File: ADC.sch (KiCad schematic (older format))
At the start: 4 parts, among them J1 RCA, J2 RCA, P1 CONN_6, P2 CONN_6

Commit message: Completed component product code specification; started on footprints.
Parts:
- J1: DigiKey (none) -> CP-1414-ND
- J2: DigiKey (none) -> CP-1413-ND
- P1: DigiKey (none) -> SC1631-ND
- P2: DigiKey (none) -> SC1738-ND
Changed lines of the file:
@@
 LIBS:my-conn
 LIBS:ADC-cache
-EELAYER 27 0
+EELAYER 24 0
 EELAYER END
 $Descr A4 11693 8268
@@
 F 2 "" H 2500 4550 60  0000 C CNN
 F 3 "" H 2500 4550 60  0000 C CNN
+F 4 "SC1631-ND" V 2500 4550 60  0001 C CNN "DigiKey"
 	1    2500 4550
 	1    0    0    -1
@@
 F 2 "" H 2900 4550 60  0000 C CNN
 F 3 "" H 2900 4550 60  0000 C CNN
+F 4 "SC1738-ND" V 2900 4550 60  0001 C CNN "DigiKey"
 	1    2900 4550
 	-1   0    0    -1
@@
 F 2 "" H 5600 1900 60  0000 C CNN
 F 3 "" H 5600 1900 60  0000 C CNN
+F 4 "CP-1414-ND" H 5600 1900 60  0001 C CNN "DigiKey"
 	1    5600 1900
 	1    0    0    -1
@@
 F 2 "" H 5600 2750 60  0000 C CNN
 F 3 "" H 5600 2750 60  0000 C CNN
+F 4 "CP-1413-ND" H 5600 2750 60  0001 C CNN "DigiKey"
 	1    5600 2750
 	1    0    0    -1

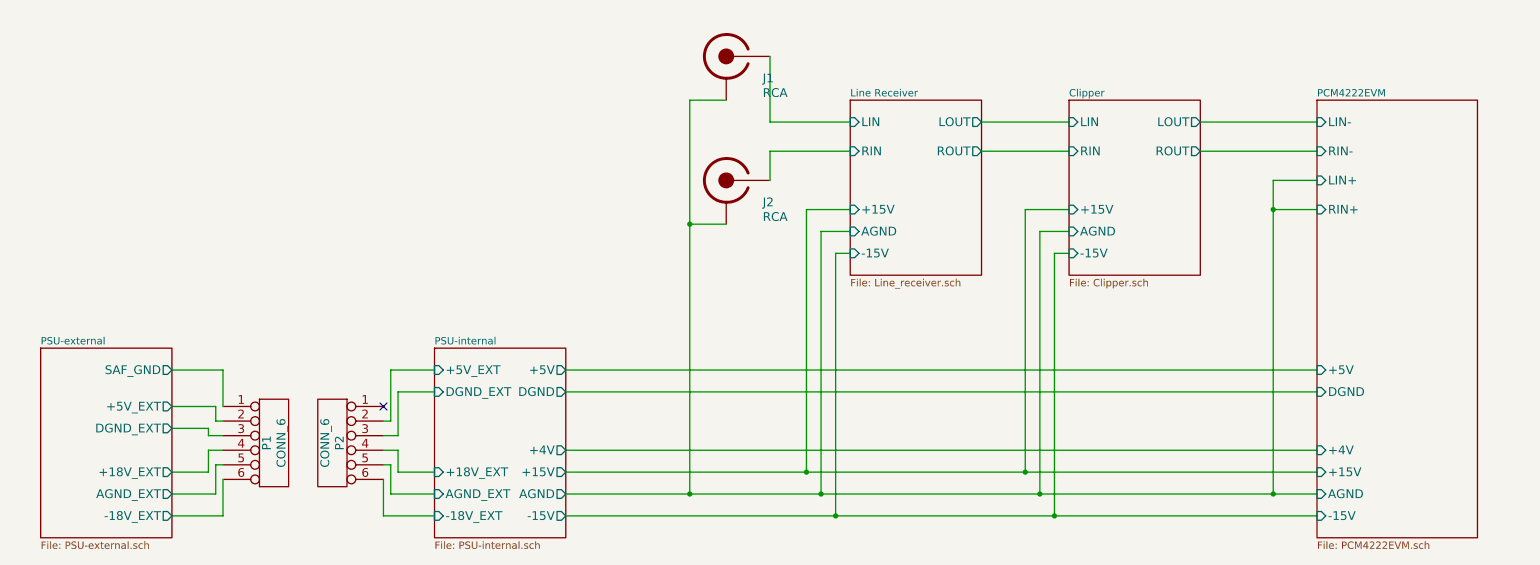
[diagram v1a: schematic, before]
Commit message: Added internal connectors; specified all footprints and part IDs except for the trafos.
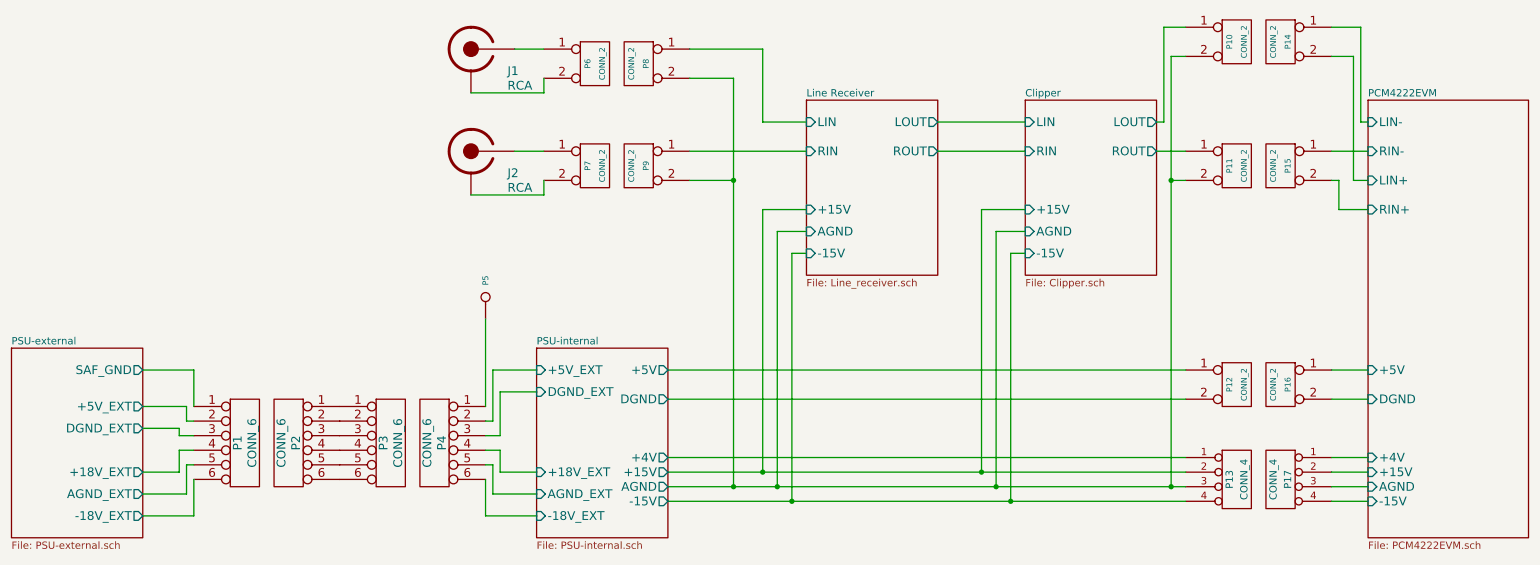
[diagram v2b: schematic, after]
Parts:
- added P10, P11, P12, P14, P15, P16, P6, P7, P8, P9: CONN_2, symbol CONN_2
- added P13, P17: CONN_4, symbol CONN_4
- added P3, P4: CONN_6, symbol CONN_6
- added P5: CONN_1, symbol CONN_1
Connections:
- net Clipper/+15V: now also P13.2 (P2)
- net Clipper/-15V: now also P13.4 (P4)
- net Clipper/AGND: now also P10.2 (PM), P11.2 (PM), P13.3 (P3), P8.2 (PM), P9.2 (PM); no longer J1.~, J2.~
- net Clipper/LOUT: now also P10.1 (P1)
- net Clipper/ROUT: now also P11.1 (P1)
- net Line Receiver/LIN: now also P8.1 (P1); no longer J1.~
- net Line Receiver/RIN: now also P9.1 (P1); no longer J2.~
- net PCM4222EVM/+4V: now also P17.1 (P1)
- net PCM4222EVM/+5V: now also P16.1 (P1)
- net PCM4222EVM/DGND: now also P16.2 (PM)
- net PSU-internal/+18V_EXT: now also P4.4; no longer P2.4
- net PSU-internal/+5V_EXT: now also P4.2; no longer P2.2
- net PSU-internal/-18V_EXT: now also P4.6; no longer P2.6
- net PSU-internal/AGND_EXT: now also P4.5; no longer P2.5
- net PSU-internal/DGND_EXT: now also P4.3; no longer P2.3
- net at P2.1: now also P3.1
- new net: P2.2, P3.2
- new net: P2.3, P3.3
- new net: P2.4, P3.4
- new net: P2.5, P3.5
- new net: P2.6, P3.6
- new net: J1.~, P6.1 (P1)
- new net: J1.~, P6.2 (PM)
- new net: J2.~, P7.1 (P1)
- new net: J2.~, P7.2 (PM)
- new net: P4.1, P5.1
- new net PCM4222EVM/+15V: P17.2 (P2)
- new net PCM4222EVM/-15V: P17.4 (P4)
- new net PCM4222EVM/AGND: P17.3 (P3)
- new net PCM4222EVM/LIN+: P14.2 (PM)
- new net PCM4222EVM/LIN-: P14.1 (P1)
- new net PCM4222EVM/RIN+: P15.2 (PM)
- new net PCM4222EVM/RIN-: P15.1 (P1)
- new net PSU-internal/+4V: P13.1 (P1)
- new net PSU-internal/+5V: P12.1 (P1)
- new net PSU-internal/DGND: P12.2 (PM)
- no-connect marks 1 -> 0
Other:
- moved on the sheet: J1, J2, P1, P2

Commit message: More footprint specification and connector additions; almost done.
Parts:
- P1, P2, P3, P4: footprint (none) -> Sockets_MOLEX_KK-System:Socket_MOLEX-KK-RM2-54mm_Lock_6pin_straight
- P10, P11, P12, P14, P15, P16, P6, P7, P8, P9: footprint (none) -> Sockets_MOLEX_KK-System:Socket_MOLEX-KK-RM2-54mm_Lock_2pin_straight
- P13, P17: footprint (none) -> Sockets_MOLEX_KK-System:Socket_MOLEX-KK-RM2-54mm_Lock_4pin_straight
- P5: footprint (none) -> Connect:1pin
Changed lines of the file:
@@
 F 0 "P1" V 2250 4550 60  0000 C CNN
 F 1 "CONN_6" V 2350 4550 60  0000 C CNN
-F 2 "" H 2300 4550 60  0000 C CNN
+F 2 "Sockets_MOLEX_KK-System:Socket_MOLEX-KK-RM2-54mm_Lock_6pin_straight" H 2300 4550 60  0001 C CNN
 F 3 "" H 2300 4550 60  0000 C CNN
 F 4 "SC1631-ND" V 2300 4550 60  0001 C CNN "DigiKey"
@@
 F 0 "P2" V 2550 4550 60  0000 C CNN
 F 1 "CONN_6" V 2650 4550 60  0000 C CNN
-F 2 "" H 2600 4550 60  0000 C CNN
+F 2 "Sockets_MOLEX_KK-System:Socket_MOLEX-KK-RM2-54mm_Lock_6pin_straight" H 2600 4550 60  0001 C CNN
 F 3 "" H 2600 4550 60  0000 C CNN
 F 4 "SC1738-ND" V 2600 4550 60  0001 C CNN "DigiKey"
@@
 F 0 "J1" H 4100 1700 60  0000 L CNN
 F 1 "RCA" H 4100 1600 60  0000 L CNN
-F 2 "" H 3850 1850 60  0000 C CNN
+F 2 "" H 3850 1850 60  0001 C CNN
 F 3 "" H 3850 1850 60  0000 C CNN
 F 4 "CP-1414-ND" H 3850 1850 60  0001 C CNN "DigiKey"
@@
 F 0 "J2" H 4100 2400 60  0000 L CNN
 F 1 "RCA" H 4100 2300 60  0000 L CNN
-F 2 "" H 3850 2550 60  0000 C CNN
+F 2 "" H 3850 2550 60  0001 C CNN
 F 3 "" H 3850 2550 60  0000 C CNN
 F 4 "CP-1413-ND" H 3850 2550 60  0001 C CNN "DigiKey"
@@
 F 0 "P6" V 4650 1950 40  0000 C CNN
 F 1 "CONN_2" V 4750 1950 40  0000 C CNN
-F 2 "" H 4700 1950 60  0000 C CNN
+F 2 "Sockets_MOLEX_KK-System:Socket_MOLEX-KK-RM2-54mm_Lock_2pin_straight" H 4700 1950 60  0001 C CNN
 F 3 "" H 4700 1950 60  0000 C CNN
 F 4 "WM2011-ND" V 4700 1950 60  0001 C CNN "DigiKey"
@@
 F 0 "P7" V 4650 2650 40  0000 C CNN
 F 1 "CONN_2" V 4750 2650 40  0000 C CNN
-F 2 "" H 4700 2650 60  0000 C CNN
+F 2 "Sockets_MOLEX_KK-System:Socket_MOLEX-KK-RM2-54mm_Lock_2pin_straight" H 4700 2650 60  0001 C CNN
 F 3 "" H 4700 2650 60  0000 C CNN
 F 4 "WM2011-ND" V 4700 2650 60  0001 C CNN "DigiKey"
@@
 F 0 "P9" V 4950 2650 40  0000 C CNN
 F 1 "CONN_2" V 5050 2650 40  0000 C CNN
-F 2 "" H 5000 2650 60  0000 C CNN
+F 2 "Sockets_MOLEX_KK-System:Socket_MOLEX-KK-RM2-54mm_Lock_2pin_straight" H 5000 2650 60  0001 C CNN
 F 3 "" H 5000 2650 60  0000 C CNN
 F 4 "WM4200-ND" V 5000 2650 60  0001 C CNN "DigiKey"
@@
 F 0 "P8" V 4950 1950 40  0000 C CNN
 F 1 "CONN_2" V 5050 1950 40  0000 C CNN
-F 2 "" H 5000 1950 60  0000 C CNN
+F 2 "Sockets_MOLEX_KK-System:Socket_MOLEX-KK-RM2-54mm_Lock_2pin_straight" H 5000 1950 60  0001 C CNN
 F 3 "" H 5000 1950 60  0000 C CNN
 F 4 "WM4200-ND" V 5000 1950 60  0001 C CNN "DigiKey"
@@
 F 0 "P5" H 4030 3550 40  0000 L CNN
 F 1 "CONN_1" H 3950 3605 30  0001 C CNN
-F 2 "" H 3950 3550 60  0000 C CNN
+F 2 "Connect:1pin" H 3950 3550 60  0001 C CNN
 F 3 "" H 3950 3550 60  0000 C CNN
 	1    3950 3550
@@
 F 0 "P10" V 9050 1800 40  0000 C CNN
 F 1 "CONN_2" V 9150 1800 40  0000 C CNN
-F 2 "" H 9100 1800 60  0000 C CNN
+F 2 "Sockets_MOLEX_KK-System:Socket_MOLEX-KK-RM2-54mm_Lock_2pin_straight" H 9100 1800 60  0001 C CNN
 F 3 "" H 9100 1800 60  0000 C CNN
 F 4 "WM4200-ND" V 9100 1800 60  0001 C CNN "DigiKey"
@@
 F 0 "P14" V 9350 1800 40  0000 C CNN
 F 1 "CONN_2" V 9450 1800 40  0000 C CNN
-F 2 "" H 9400 1800 60  0000 C CNN
+F 2 "Sockets_MOLEX_KK-System:Socket_MOLEX-KK-RM2-54mm_Lock_2pin_straight" H 9400 1800 60  0001 C CNN
 F 3 "" H 9400 1800 60  0000 C CNN
 F 4 "WM2011-ND" V 9400 1800 60  0001 C CNN "DigiKey"
@@
 F 0 "P12" V 9050 4150 40  0000 C CNN
 F 1 "CONN_2" V 9150 4150 40  0000 C CNN
-F 2 "" H 9100 4150 60  0000 C CNN
+F 2 "Sockets_MOLEX_KK-System:Socket_MOLEX-KK-RM2-54mm_Lock_2pin_straight" H 9100 4150 60  0001 C CNN
 F 3 "" H 9100 4150 60  0000 C CNN
 F 4 "WM4200-ND" V 9100 4150 60  0001 C CNN "DigiKey"
@@
 F 0 "P15" V 9350 2650 40  0000 C CNN
 F 1 "CONN_2" V 9450 2650 40  0000 C CNN
-F 2 "" H 9400 2650 60  0000 C CNN
+F 2 "Sockets_MOLEX_KK-System:Socket_MOLEX-KK-RM2-54mm_Lock_2pin_straight" H 9400 2650 60  0001 C CNN
 F 3 "" H 9400 2650 60  0000 C CNN
 F 4 "WM2011-ND" V 9400 2650 60  0001 C CNN "DigiKey"
@@
 F 0 "P16" V 9350 4150 40  0000 C CNN
 F 1 "CONN_2" V 9450 4150 40  0000 C CNN
-F 2 "" H 9400 4150 60  0000 C CNN
+F 2 "Sockets_MOLEX_KK-System:Socket_MOLEX-KK-RM2-54mm_Lock_2pin_straight" H 9400 4150 60  0001 C CNN
 F 3 "" H 9400 4150 60  0000 C CNN
 F 4 "WM2011-ND" V 9400 4150 60  0001 C CNN "DigiKey"
@@
 F 0 "P11" V 9050 2650 40  0000 C CNN
 F 1 "CONN_2" V 9150 2650 40  0000 C CNN
-F 2 "" H 9100 2650 60  0000 C CNN
+F 2 "Sockets_MOLEX_KK-System:Socket_MOLEX-KK-RM2-54mm_Lock_2pin_straight" H 9100 2650 60  0001 C CNN
 F 3 "" H 9100 2650 60  0000 C CNN
 F 4 "WM4200-ND" V 9100 2650 60  0001 C CNN "DigiKey"
@@
 F 0 "P13" V 9050 4800 50  0000 C CNN
 F 1 "CONN_4" V 9150 4800 50  0000 C CNN
-F 2 "" H 9100 4800 60  0000 C CNN
+F 2 "Sockets_MOLEX_KK-System:Socket_MOLEX-KK-RM2-54mm_Lock_4pin_straight" H 9100 4800 60  0001 C CNN
 F 3 "" H 9100 4800 60  0000 C CNN
 F 4 "WM4202-ND" V 9100 4800 60  0001 C CNN "DigiKey"
@@
 F 0 "P17" V 9350 4800 50  0000 C CNN
 F 1 "CONN_4" V 9450 4800 50  0000 C CNN
-F 2 "" H 9400 4800 60  0000 C CNN
+F 2 "Sockets_MOLEX_KK-System:Socket_MOLEX-KK-RM2-54mm_Lock_4pin_straight" H 9400 4800 60  0001 C CNN
 F 3 "" H 9400 4800 60  0000 C CNN
 F 4 "WM2603-ND" V 9400 4800 60  0001 C CNN "DigiKey"
@@
 F 0 "P4" V 3550 4550 60  0000 C CNN
 F 1 "CONN_6" V 3650 4550 60  0000 C CNN
-F 2 "" H 3600 4550 60  0000 C CNN
+F 2 "Sockets_MOLEX_KK-System:Socket_MOLEX-KK-RM2-54mm_Lock_6pin_straight" H 3600 4550 60  0001 C CNN
 F 3 "" H 3600 4550 60  0000 C CNN
 F 4 "WM4204-ND" V 3600 4550 60  0001 C CNN "DigiKey"
@@
 F 0 "P3" V 3250 4550 60  0000 C CNN
 F 1 "CONN_6" V 3350 4550 60  0000 C CNN
-F 2 "" H 3300 4550 60  0000 C CNN
+F 2 "Sockets_MOLEX_KK-System:Socket_MOLEX-KK-RM2-54mm_Lock_6pin_straight" H 3300 4550 60  0001 C CNN
 F 3 "" H 3300 4550 60  0000 C CNN
 F 4 "WM2015-ND" V 3300 4550 60  0001 C CNN "DigiKey"

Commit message: Changed to use the fixed IEC socket device; the PSU netlist should now be (more) correct.
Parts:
- J1, J2: footprint (none) -> Oddities:Dummy_Empty
- P14, P15, P16, P6, P7: footprint Sockets_MOLEX_KK-System:Socket_MOLEX-KK-RM2-54mm_Lock_2pin_straight -> Oddities:Dummy_Empty
- P17: footprint Sockets_MOLEX_KK-System:Socket_MOLEX-KK-RM2-54mm_Lock_4pin_straight -> Oddities:Dummy_Empty
- P2, P3: footprint Sockets_MOLEX_KK-System:Socket_MOLEX-KK-RM2-54mm_Lock_6pin_straight -> Oddities:Dummy_Empty
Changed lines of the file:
@@
 F 0 "P2" V 2550 4550 60  0000 C CNN
 F 1 "CONN_6" V 2650 4550 60  0000 C CNN
-F 2 "Sockets_MOLEX_KK-System:Socket_MOLEX-KK-RM2-54mm_Lock_6pin_straight" H 2600 4550 60  0001 C CNN
+F 2 "Oddities:Dummy_Empty" H 2600 4550 60  0001 C CNN
 F 3 "" H 2600 4550 60  0000 C CNN
 F 4 "SC1738-ND" V 2600 4550 60  0001 C CNN "DigiKey"
@@
 F 0 "J1" H 4100 1700 60  0000 L CNN
 F 1 "RCA" H 4100 1600 60  0000 L CNN
-F 2 "" H 3850 1850 60  0001 C CNN
+F 2 "Oddities:Dummy_Empty" H 3850 1850 60  0001 C CNN
 F 3 "" H 3850 1850 60  0000 C CNN
 F 4 "CP-1414-ND" H 3850 1850 60  0001 C CNN "DigiKey"
@@
 F 0 "J2" H 4100 2400 60  0000 L CNN
 F 1 "RCA" H 4100 2300 60  0000 L CNN
-F 2 "" H 3850 2550 60  0001 C CNN
+F 2 "Oddities:Dummy_Empty" H 3850 2550 60  0001 C CNN
 F 3 "" H 3850 2550 60  0000 C CNN
 F 4 "CP-1413-ND" H 3850 2550 60  0001 C CNN "DigiKey"
@@
 F 0 "P6" V 4650 1950 40  0000 C CNN
 F 1 "CONN_2" V 4750 1950 40  0000 C CNN
-F 2 "Sockets_MOLEX_KK-System:Socket_MOLEX-KK-RM2-54mm_Lock_2pin_straight" H 4700 1950 60  0001 C CNN
+F 2 "Oddities:Dummy_Empty" H 4700 1950 60  0001 C CNN
 F 3 "" H 4700 1950 60  0000 C CNN
 F 4 "WM2011-ND" V 4700 1950 60  0001 C CNN "DigiKey"
@@
 F 0 "P7" V 4650 2650 40  0000 C CNN
 F 1 "CONN_2" V 4750 2650 40  0000 C CNN
-F 2 "Sockets_MOLEX_KK-System:Socket_MOLEX-KK-RM2-54mm_Lock_2pin_straight" H 4700 2650 60  0001 C CNN
+F 2 "Oddities:Dummy_Empty" H 4700 2650 60  0001 C CNN
 F 3 "" H 4700 2650 60  0000 C CNN
 F 4 "WM2011-ND" V 4700 2650 60  0001 C CNN "DigiKey"
@@
 F 0 "P14" V 9350 1800 40  0000 C CNN
 F 1 "CONN_2" V 9450 1800 40  0000 C CNN
-F 2 "Sockets_MOLEX_KK-System:Socket_MOLEX-KK-RM2-54mm_Lock_2pin_straight" H 9400 1800 60  0001 C CNN
+F 2 "Oddities:Dummy_Empty" H 9400 1800 60  0001 C CNN
 F 3 "" H 9400 1800 60  0000 C CNN
 F 4 "WM2011-ND" V 9400 1800 60  0001 C CNN "DigiKey"
@@
 F 0 "P15" V 9350 2650 40  0000 C CNN
 F 1 "CONN_2" V 9450 2650 40  0000 C CNN
-F 2 "Sockets_MOLEX_KK-System:Socket_MOLEX-KK-RM2-54mm_Lock_2pin_straight" H 9400 2650 60  0001 C CNN
+F 2 "Oddities:Dummy_Empty" H 9400 2650 60  0001 C CNN
 F 3 "" H 9400 2650 60  0000 C CNN
 F 4 "WM2011-ND" V 9400 2650 60  0001 C CNN "DigiKey"
@@
 F 0 "P16" V 9350 4150 40  0000 C CNN
 F 1 "CONN_2" V 9450 4150 40  0000 C CNN
-F 2 "Sockets_MOLEX_KK-System:Socket_MOLEX-KK-RM2-54mm_Lock_2pin_straight" H 9400 4150 60  0001 C CNN
+F 2 "Oddities:Dummy_Empty" H 9400 4150 60  0001 C CNN
 F 3 "" H 9400 4150 60  0000 C CNN
 F 4 "WM2011-ND" V 9400 4150 60  0001 C CNN "DigiKey"
@@
 F 0 "P17" V 9350 4800 50  0000 C CNN
 F 1 "CONN_4" V 9450 4800 50  0000 C CNN
-F 2 "Sockets_MOLEX_KK-System:Socket_MOLEX-KK-RM2-54mm_Lock_4pin_straight" H 9400 4800 60  0001 C CNN
+F 2 "Oddities:Dummy_Empty" H 9400 4800 60  0001 C CNN
 F 3 "" H 9400 4800 60  0000 C CNN
 F 4 "WM2603-ND" V 9400 4800 60  0001 C CNN "DigiKey"
@@
 F 0 "P3" V 3250 4550 60  0000 C CNN
 F 1 "CONN_6" V 3350 4550 60  0000 C CNN
-F 2 "Sockets_MOLEX_KK-System:Socket_MOLEX-KK-RM2-54mm_Lock_6pin_straight" H 3300 4550 60  0001 C CNN
+F 2 "Oddities:Dummy_Empty" H 3300 4550 60  0001 C CNN
 F 3 "" H 3300 4550 60  0000 C CNN
 F 4 "WM2015-ND" V 3300 4550 60  0001 C CNN "DigiKey"

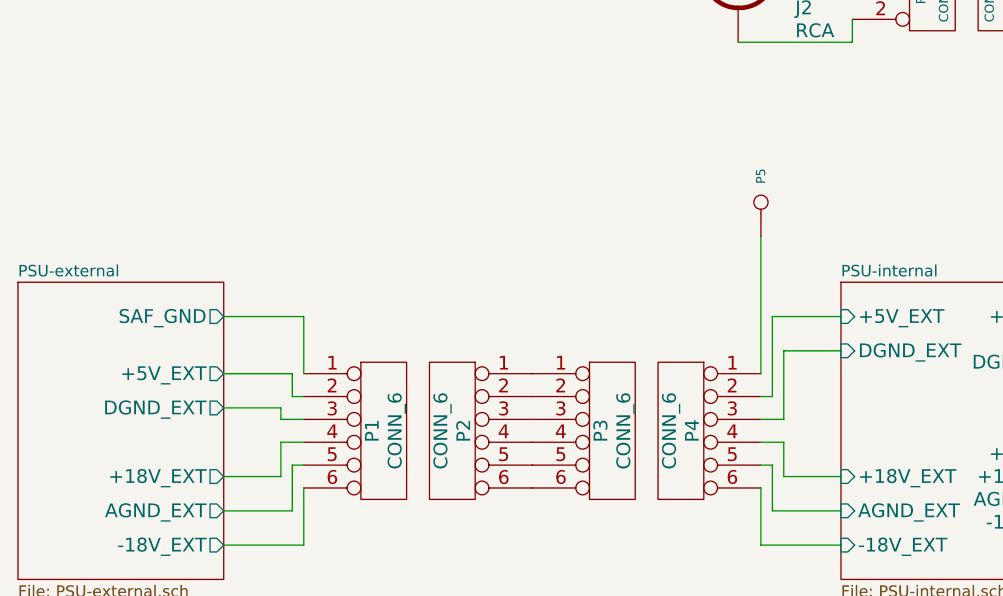
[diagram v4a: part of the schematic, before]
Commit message: A lot of routing, some parts changes:   * Added snubber C/RC snubbers to transformer secondaries.   * Changed PSU OA from OPA209 to OPA27.   * Routed external PSU.   * Mostly done routing internal circuits.  Just need to get everything together.   * Changed digital transformer to a more appropriately-specced one.
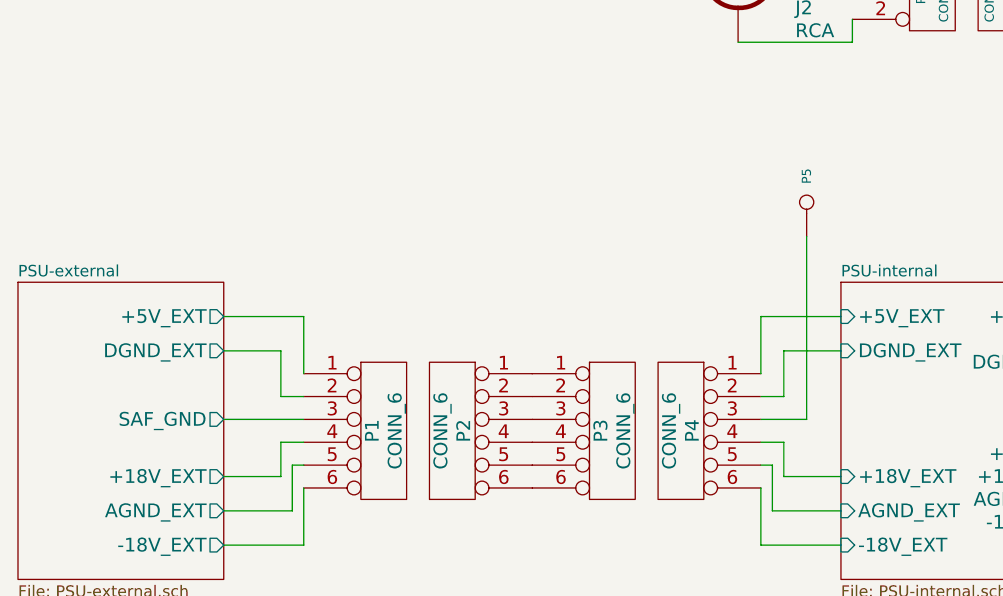
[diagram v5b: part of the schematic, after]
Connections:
- net PSU-external/+5V_EXT: now also P1.1; no longer P1.2
- net PSU-external/DGND_EXT: now also P1.2; no longer P1.3
- net PSU-external/SAF_GND: now also P1.3; no longer P1.1
- net PSU-internal/+5V_EXT: now also P4.1; no longer P4.2
- net PSU-internal/DGND_EXT: now also P4.2; no longer P4.3
- net at P5.1: now also P4.3; no longer P4.1
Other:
- moved on the sheet: P5
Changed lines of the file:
@@
 F0 "PSU-external" 50
 F1 "PSU-external.sch" 50
-F2 "+5V_EXT" O R 1600 4300 60
+F2 "+5V_EXT" O R 1600 4050 60
 F3 "+18V_EXT" O R 1600 4750 60
 F4 "AGND_EXT" O R 1600 4900 60
 F5 "-18V_EXT" O R 1600 5050 60
-F6 "DGND_EXT" O R 1600 4450 60
-F7 "SAF_GND" O R 1600 4050 60
+F6 "DGND_EXT" O R 1600 4200 60
+F7 "SAF_GND" O R 1600 4500 60
 $EndSheet
 $Comp
@@
 L CONN_1 P5
 U 1 1 538818A0
-P 3950 3550
-F 0 "P5" H 4030 3550 40  0000 L CNN
-F 1 "CONN_1" H 3950 3605 30  0001 C CNN
-F 2 "Connect:1pin" H 3950 3550 60  0001 C CNN
-F 3 "" H 3950 3550 60  0000 C CNN
-	1    3950 3550
+P 4150 3550
+F 0 "P5" H 4230 3550 40  0000 L CNN
+F 1 "CONN_1" H 4150 3605 30  0001 C CNN
+F 2 "Connect:1pin" H 4150 3550 60  0001 C CNN
+F 3 "" H 4150 3550 60  0000 C CNN
+	1    4150 3550
 	0    -1   -1   0
 $EndComp
@@
 $EndComp
 Wire Wire Line
-	1600 4050 1950 4050
-Wire Wire Line
-	1950 4050 1950 4300
-Wire Wire Line
-	1600 4300 1900 4300
-Wire Wire Line
-	1900 4300 1900 4400
-Wire Wire Line
-	1900 4400 1950 4400
-Wire Wire Line
-	1600 4450 1850 4450
-Wire Wire Line
-	1850 4450 1850 4500
-Wire Wire Line
-	1850 4500 1950 4500
-Wire Wire Line
 	1600 4750 1850 4750
 Wire Wire Line
@@
 	4050 4600 4050 4750
 Wire Wire Line
-	4050 4200 4050 4500
-Wire Wire Line
-	4050 4500 3950 4500
-Wire Wire Line
-	4000 4400 3950 4400
-Wire Wire Line
-	4000 4050 4000 4400
-Wire Wire Line
 	4050 4750 4300 4750
 Wire Wire Line
@@
 	7650 2550 7050 2550
 Wire Wire Line
-	4300 4200 4050 4200
-Wire Wire Line
-	4000 4050 4300 4050
-Wire Wire Line
 	4350 1850 4150 1850
 Wire Wire Line
@@
 Wire Wire Line
 	5850 1850 5850 2350
-Wire Wire Line
-	3950 3700 3950 4300
 Wire Wire Line
 	5850 1850 5350 1850
@@
 Wire Wire Line
 	9800 2950 10000 2950
+Wire Wire Line
+	1600 4500 1950 4500
+Wire Wire Line
+	3950 4500 4150 4500
+Wire Wire Line
+	4150 4500 4150 3700
+Wire Wire Line
+	1600 4050 1950 4050
+Wire Wire Line
+	1950 4050 1950 4300
+Wire Wire Line
+	1950 4400 1850 4400
+Wire Wire Line
+	1850 4400 1850 4200
+Wire Wire Line
+	1850 4200 1600 4200
+Wire Wire Line
+	3950 4300 3950 4050
+Wire Wire Line
+	3950 4050 4300 4050
+Wire Wire Line
+	3950 4400 4050 4400
+Wire Wire Line
+	4050 4400 4050 4200
+Wire Wire Line
+	4050 4200 4300 4200
 $EndSCHEMATC

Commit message: First complete version.   * Added 10uF decoupling capacitors to the start of each signal processing section.   * Completed routing.  A few -18 V nets remain unrouted; these will be wired in.
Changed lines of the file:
@@
 	5200 4750 8750 4750
-Wire Wire Line
-	5850 2950 5850 4750
-Wire Wire Line
-	5200 4850 8750 4850
 Wire Wire Line
 	5200 4950 8750 4950
@@
 Wire Wire Line
 	7350 2950 7350 4750
-Connection ~ 5850 4750
 Connection ~ 7550 4950
 Connection ~ 7450 4850
 Connection ~ 7350 4750
-Wire Wire Line
-	8750 4650 5200 4650
 Wire Wire Line
 	5200 4250 8750 4250
@@
 Wire Wire Line
 	9750 4250 10000 4250
-Wire Wire Line
-	9750 4650 10000 4650
-Wire Wire Line
-	10000 4750 9750 4750
-Wire Wire Line
-	9750 4850 10000 4850
 Wire Wire Line
 	10000 4950 9750 4950
@@
 Wire Wire Line
 	4050 4200 4300 4200
+Connection ~ 5850 4750
+Wire Wire Line
+	5850 2950 5850 4750
+Wire Wire Line
+	5200 4850 8750 4850
+Wire Wire Line
+	5200 4650 8750 4650
+Wire Wire Line
+	9750 4650 10000 4650
+Wire Wire Line
+	9750 4850 10000 4850
+Wire Wire Line
+	9750 4750 10000 4750
 $EndSCHEMATC
